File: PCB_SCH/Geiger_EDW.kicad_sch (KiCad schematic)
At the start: 44 parts, among them J1 Power, J2 +5V Output, J3 STS-5, J4 Piezo, J5 Output, P1 500k, Q1 IRF7404, Q2 BC857, Q3 IRFBC40SPBF, Q4 BC847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

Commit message: Update Geiger_EDW.kicad_sch
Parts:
- R2: value 4 -> 2
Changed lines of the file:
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@@
       (effects (font (size 1.27 1.27)))
     )
-    (property "Value" "4" (at 48.26 16.51 90)
+    (property "Value" "2" (at 48.26 16.51 90)
       (effects (font (size 1.27 1.27)))
     )

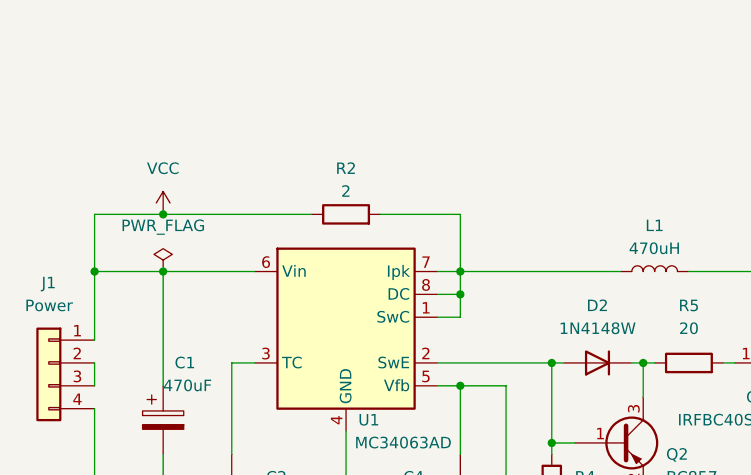
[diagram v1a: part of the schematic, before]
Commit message: Update R2 value
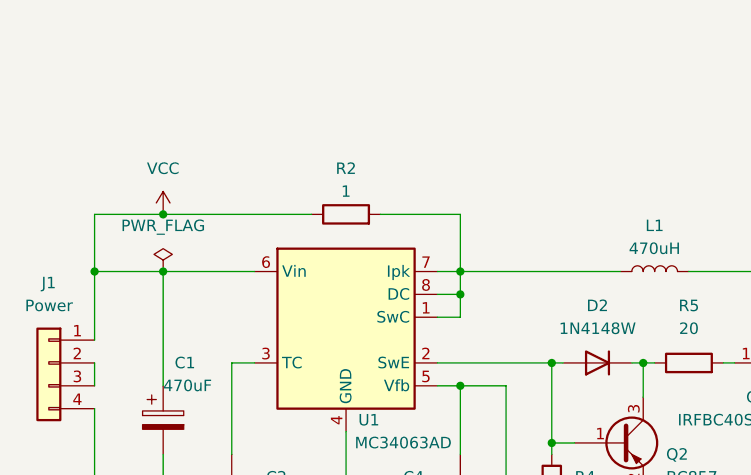
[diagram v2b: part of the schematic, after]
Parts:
- R2: value 2 -> 1
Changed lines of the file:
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@@
       (effects (font (size 1.27 1.27)))
     )
-    (property "Value" "2" (at 48.26 16.51 90)
+    (property "Value" "1" (at 48.26 16.51 90)
       (effects (font (size 1.27 1.27)))
     )

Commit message: Revert "Update R2 value"
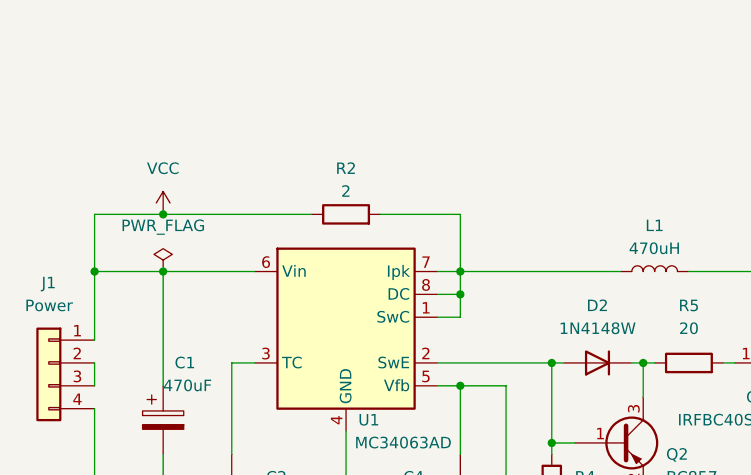
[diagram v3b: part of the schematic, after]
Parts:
- R2: value 1 -> 2
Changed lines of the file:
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@@
       (effects (font (size 1.27 1.27)))
     )
-    (property "Value" "1" (at 48.26 16.51 90)
+    (property "Value" "2" (at 48.26 16.51 90)
       (effects (font (size 1.27 1.27)))
     )

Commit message: another r2 change
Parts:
- R2: value 2 -> 4
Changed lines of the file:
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@@
       (effects (font (size 1.27 1.27)))
     )
-    (property "Value" "2" (at 48.26 16.51 90)
+    (property "Value" "4" (at 48.26 16.51 90)
       (effects (font (size 1.27 1.27)))
     )
